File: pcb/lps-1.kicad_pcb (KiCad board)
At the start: 4 copper layers, 75.8 x 30 mm, 24 parts, among them J1 Conn_01x12_Pin, J15 PWR, J2 Conn_01x06_Pin, J4 A_INA219, J5 XBEE, J6 DEV, U1 TC1262-33, U2 ATMega1608_32

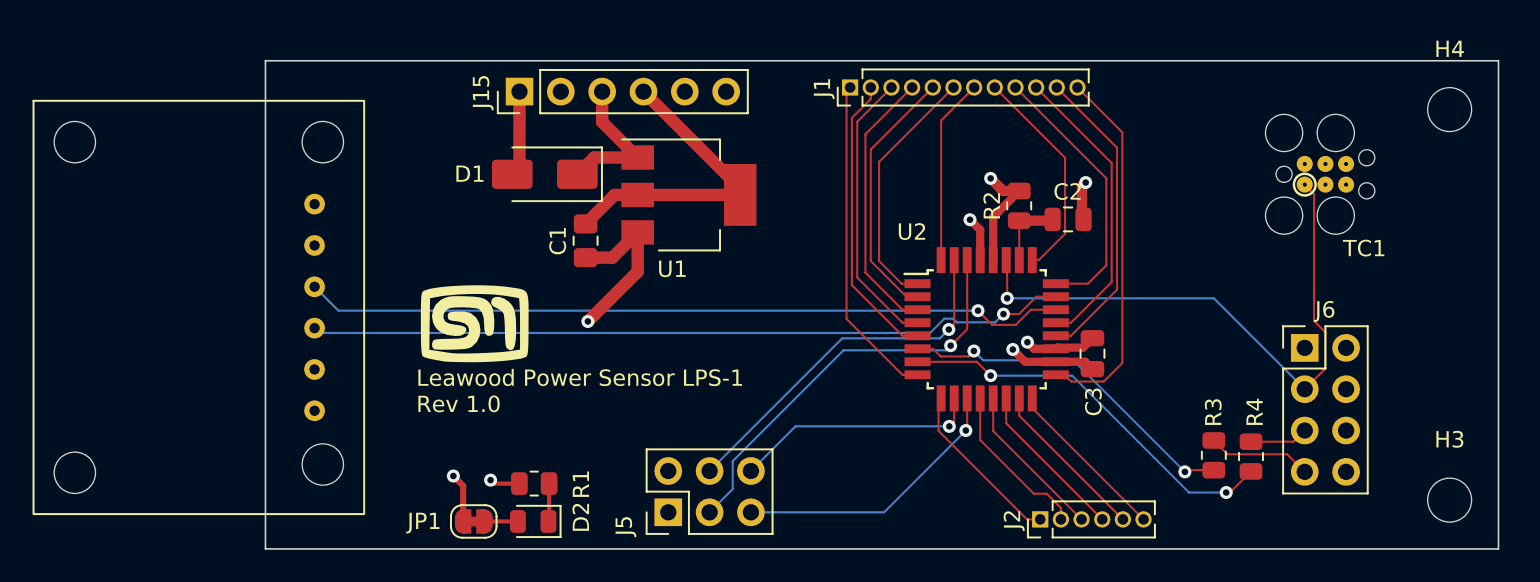
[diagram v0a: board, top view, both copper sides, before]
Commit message: Refactored the connectors for the LPS-X-1
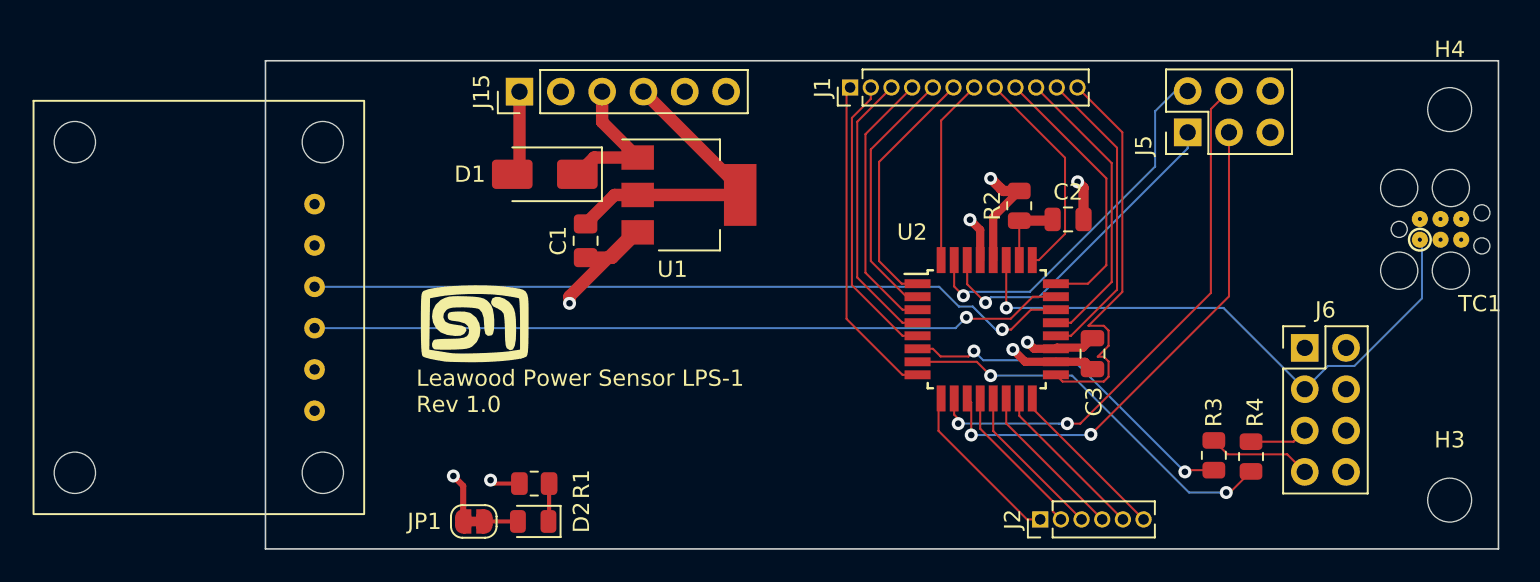
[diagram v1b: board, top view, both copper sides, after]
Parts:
- moved J5 39.5 mm to (125.9, 59.4)
- moved TC1 7.84 mm to (140.2, 66.0)
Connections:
- J5 pad 1: +3.3V -> /TxD0
- J5 pad 2: GND -> /RxD0
- J5 pad 3: /TxD0 -> /MODEM_SLEEP
- J5 pad 4: /RxD0 -> /MODEM_RESET
- J5 pad 5: /MODEM_SLEEP -> +3.3V
- J5 pad 6: /MODEM_RESET -> GND
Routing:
- net /MODEM_RESET: track 15.2 -> 33.4 mm, vias 1 -> 2
- net /MODEM_SLEEP: track 17.3 -> 31.8 mm, vias 1 -> 2
- net /TxD0: track 25.7 -> 20.4 mm
- net /PD7: track 22.8 -> 25.1 mm
- net /RxD0: track 22.7 -> 23.4 mm
- net +3.3V: track 26.0 -> 25.5 mm

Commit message: Reduces the board footprint and introduces copper fills on F and B
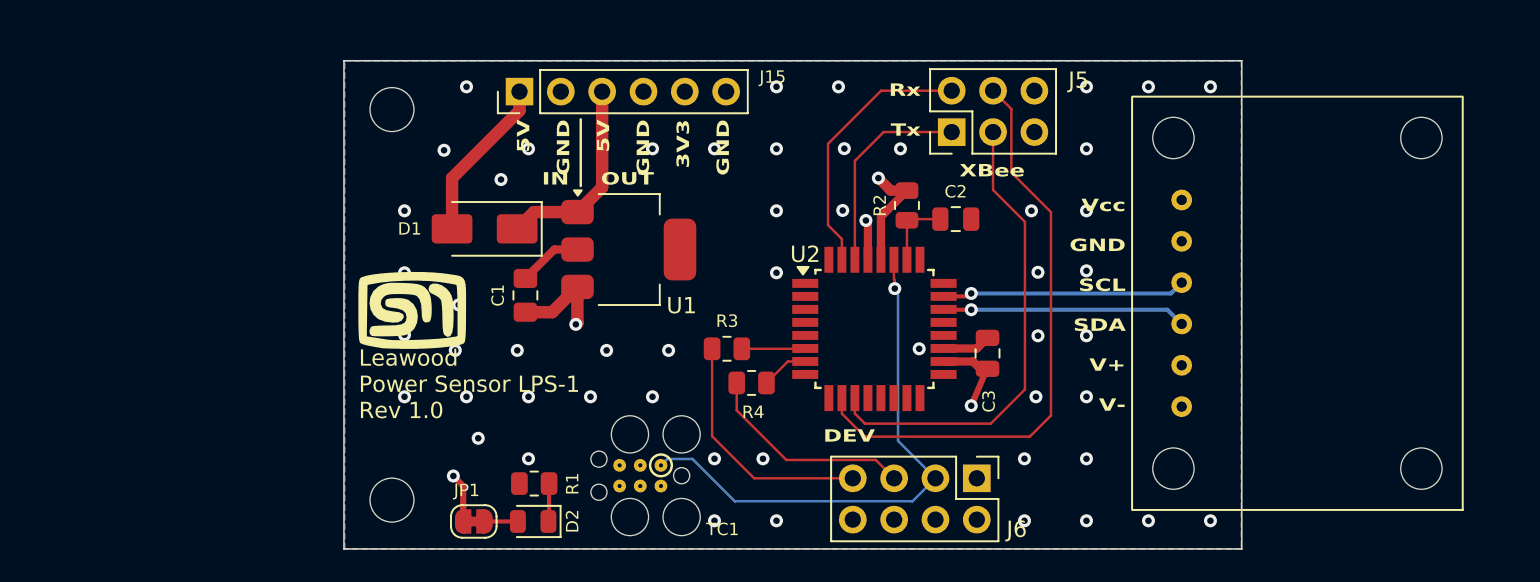
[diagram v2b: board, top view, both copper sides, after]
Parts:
- removed J1: Conn_01x12_Pin, Connector_PinHeader_1.27mm:PinHeader_1x12_P1.27mm_Vertical
- removed J2: Conn_01x06_Pin, Connector_PinHeader_1.27mm:PinHeader_1x06_P1.27mm_Vertical
- moved J4 91.4 mm to (142.8, 82.6), turned to 180 degrees
- moved H3 65.0 mm to (77.0, 82.0)
- moved H4 65.0 mm to (77.0, 58.0)
- moved TC1 48.7 mm to (93.5, 79.9), turned to 180 degrees
- moved Lg3 34.0 mm to (76.3, 69.7), turned to 90 degrees
- moved R4 31.0 mm to (99.1, 74.8), turned to 180 degrees
- moved R3 30.6 mm to (97.6, 72.7), turned to 180 degrees
- moved J6 21.7 mm to (112.9, 80.7), turned to -90 degrees
- moved Lg1 16.3 mm to (114.3, 71.3)
- moved J5 14.5 mm to (111.4, 59.4)
- moved C2 6.90 mm to (111.7, 64.7)
- moved R2 6.90 mm to (108.7, 63.9)
- moved U2 6.90 mm to (106.7, 71.5)
- moved C3 6.45 mm to (113.6, 73.0)
- moved C1 4.99 mm to (85.2, 69.4)
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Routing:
- net /SDA: track 47.2 -> 15.0 mm
- net /SCL: track 46.4 -> 15.0 mm
- net /PD7: track 25.1 -> 0.00 mm
- net Net-(U2-PC1/RxD1-IN1): track 24.4 -> 2.93 mm, vias 2 -> 0
- net GND: track 30.5 -> 9.37 mm, vias 4 -> 53
- net /PC2: track 20.1 -> 0.00 mm
- net /PF0: track 18.9 -> 0.00 mm
- net /PF1: track 18.3 -> 0.00 mm
- net /SS: track 18.0 -> 0.00 mm
- net Net-(U2-PC0/TxD1/2-WO/1-IN0): track 21.7 -> 3.91 mm, vias 2 -> 0
- net /SCK: track 17.4 -> 0.00 mm
- net /PF4: track 16.8 -> 0.00 mm
- net /MISO: track 16.7 -> 0.00 mm
- net /MOSI: track 16.0 -> 0.00 mm
- net /PA3: track 15.5 -> 0.00 mm
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- added copper zone on B.Cu, net GND
- added copper zone on F.Cu, net GND
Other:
- board size 75.8 x 30 mm -> 55.2 x 30 mm
- board text added: "5V GND 5V GND 3V3 GND"
- board text added: "DEV"
- board text added: "IN OUT"
- board text added: "Rx Tx"
- board text added: "Vcc GND SCL SDA V+ V-"
- board text added: "XBee"

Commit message: Rework to include a 5V LDO
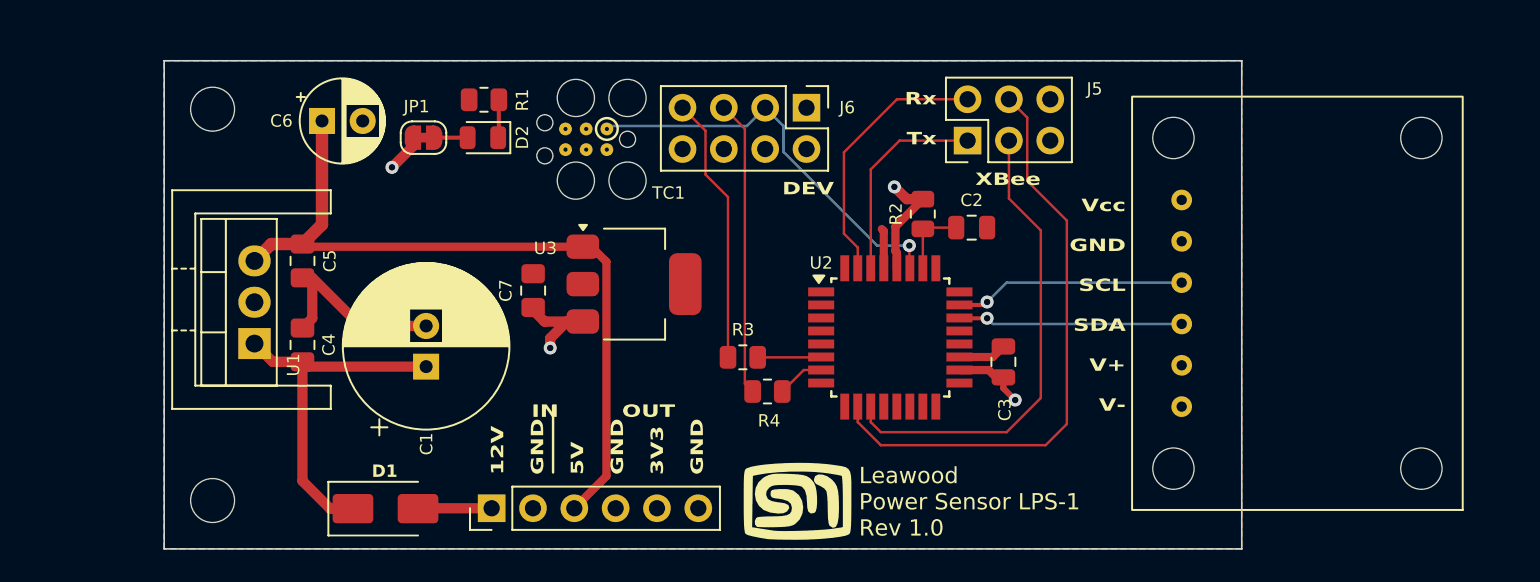
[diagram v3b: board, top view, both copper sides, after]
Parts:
- added C4: 0.1μF, Capacitor_SMD:C_0805_2012Metric_Pad1.18x1.45mm_HandSolder, F.Cu at (71.5, 72.5)
- added C5: 0.1μF, Capacitor_SMD:C_0805_2012Metric_Pad1.18x1.45mm_HandSolder, F.Cu at (71.5, 67.3)
- added C6: 10μF, Capacitor_THT:CP_Radial_D5.0mm_P2.50mm, F.Cu at (72.7, 58.7)
- added C7: 1μF, Capacitor_SMD:C_0805_2012Metric_Pad1.18x1.45mm_HandSolder, F.Cu at (85.7, 69.1)
- added HS1: Heatsink, lps-1-Footprints:Wakefield-E274_13.1x19.3mm, F.Cu at (63.6, 69.7)
- added U3: TC1262-33, Package_TO_SOT_SMD:SOT-223-3_TabPin2, F.Cu at (91.9, 68.7)
- C1: value 1μF -> 220μF; footprint Capacitor_SMD:C_0805_2012Metric_Pad1.18x1.45mm_HandSolder -> Capacitor_THT:CP_Radial_D10.0mm_P2.50mm
- U1: value TC1262-33 -> L7805; footprint Package_TO_SOT_SMD:SOT-223-3_TabPin2 -> Package_TO_SOT_THT:TO-220-3_Vertical
- moved Lg3 41.0 mm to (115.2, 82.4), turned to 180 degrees
- moved Lg2 26.4 mm to (101.9, 82.0)
- moved J15 25.7 mm to (83.1, 82.5)
- moved J6 25.1 mm to (102.5, 57.9)
- moved D2 23.8 mm to (82.6, 59.7)
- moved JP1 23.8 mm to (78.9, 59.7)
- moved R1 23.8 mm to (82.7, 57.4)
- moved U1 23.7 mm to (68.5, 72.4), turned to 90 degrees
- moved TC1 20.9 mm to (90.2, 59.2)
- moved D1 18.2 mm to (76.6, 82.5), turned to 0 degrees
- moved H3 11.0 mm to (66.0, 82.0)
- moved H4 11.0 mm to (66.0, 58.0)
- moved C1 7.51 mm to (79.1, 73.8)
- moved Lg1 1.11 mm to (115.3, 71.8)
- moved R4 1.11 mm to (100.1, 75.3)
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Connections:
- net /5VIN renamed /12VIN
- C1 pad 1: +3.3V -> Net-(D1-K)
- D1 pad 1: +5V -> Net-(D1-K)
- U1 pad 1: +5V -> Net-(D1-K)
- U1 pad 3: +3.3V -> +5V
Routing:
- net +5V: track 12.2 -> 46.5 mm
- net Net-(D1-K): track 0.00 -> 22.3 mm
- net /UPDI: track 33.2 -> 25.0 mm
- net GND: track 9.37 -> 17.0 mm, vias 53 -> 0
- net /12VIN: track 10.2 -> 4.54 mm
- net /DIN: track 13.1 -> 18.2 mm
- net /DOUT: track 15.1 -> 16.5 mm
- net /SDA: track 15.0 -> 13.8 mm
- net +3.3V: track 21.2 -> 20.1 mm
- net /SCL: track 15.0 -> 14.2 mm
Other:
- board size 55.2 x 30 mm -> 66.2 x 30 mm
- board text added: "12V GND 5V GND 3V3 GND"
- board text removed: "5V GND 5V GND 3V3 GND"

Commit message: Reworked the connectors
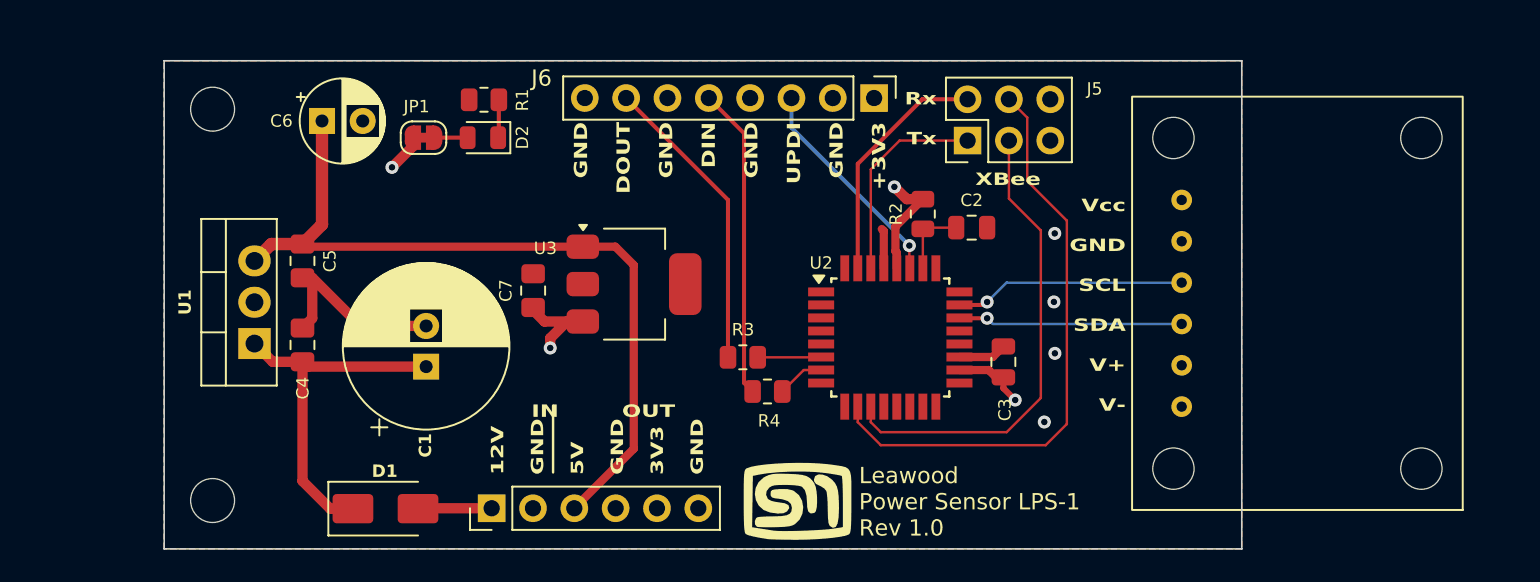
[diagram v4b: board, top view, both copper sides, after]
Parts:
- removed HS1: Heatsink, lps-1-Footprints:Wakefield-E274_13.1x19.3mm
- removed TC1: ISP, TagConnect:PRG_TC2030-IDC-FP_TH
- J6: footprint Connector_PinHeader_2.54mm:PinHeader_2x04_P2.54mm_Vertical -> Connector_PinHeader_2.54mm:PinHeader_1x08_P2.54mm_Vertical
- moved J6 4.20 mm to (106.6, 57.3)
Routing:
- net /UPDI: track 25.0 -> 13.5 mm
- net +5V: track 46.5 -> 48.8 mm
- net /DOUT: track 16.5 -> 18.5 mm
- net /RxD0: track 16.4 -> 14.8 mm
- net /DIN: track 18.2 -> 19.2 mm
- net GND: vias 0 -> 4
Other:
- board text added: "GND DOUT GND DIN GND UPDI GND +3V3"
- board text removed: "DEV"

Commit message: Revision 1.0
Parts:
- J4: footprint lps-1-Footprints:Adafruit-INA219 -> lps-1-Footprints:Adafruit-INA219_2xM2.5
- moved J4 25.7 mm to (125.5, 63.5)
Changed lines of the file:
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@@
 		)
 	)
-	(footprint "lps-1-Footprints:Adafruit-INA219"
+	(footprint "lps-1-Footprints:Adafruit-INA219_2xM2.5"
 		(layer "F.Cu")
-		(at 142.80435 82.605 180)
+		(at 125.524 63.55 180)
 		(property "Reference" "J4"
-			(at 2.54 27.94 180)
+			(at 2.159 7.493 180)
 			(layer "Dwgs.User")
 			(hide yes)
@@
 		)
 		(property "Value" "A_INA219"
-			(at 10.16 12.7 -90)
+			(at 4.064 -6.35 -90)
 			(layer "F.Fab")
 			(effects
@@
 			)
 		)
-		(property "Footprint" "lps-1-Footprints:Adafruit-INA219"
+		(property "Footprint" "lps-1-Footprints:Adafruit-INA219_2xM2.5"
 			(at 0 0 180)
 			(unlocked yes)
@@
 		(attr through_hole)
 		(fp_rect
-			(start 0 0)
-			(end 20.32 25.4)
+			(start -1.794 -19.05)
+			(end 3.032 6.35)
 			(stroke
 				(width 0.12)
@@
 		)
 		(pad "" np_thru_hole circle
-			(at 2.54 2.54 180)
+			(at 0.492 -16.51 180)
 			(size 2.54 2.54)
 			(drill 2.54)
@@
 		)
 		(pad "" np_thru_hole circle
-			(at 2.54 22.86 180)
-			(size 2.54 2.54)
-			(drill 2.54)
-			(layers "F&B.Cu" "*.Mask")
-		)
-		(pad "" np_thru_hole circle
-			(at 17.78 2.54 180)
-			(size 2.54 2.54)
-			(drill 2.54)
-			(layers "F&B.Cu" "*.Mask")
-		)
-		(pad "" np_thru_hole circle
-			(at 17.78 22.86 180)
+			(at 0.492 3.81 180)
 			(size 2.54 2.54)
 			(drill 2.54)
@@
 		)
 		(pad "1" thru_hole circle
-			(at 17.272 19.05 180)
+			(at -0.016 0 180)
 			(size 1.27 1.27)
 			(drill 0.635)
@@
 		)
 		(pad "2" thru_hole circle
-			(at 17.272 16.51 180)
+			(at -0.016 -2.54 180)
 			(size 1.27 1.27)
 			(drill 0.635)
@@
 		)
 		(pad "3" thru_hole circle
-			(at 17.272 13.97 180)
+			(at -0.016 -5.08 180)
 			(size 1.27 1.27)
 			(drill 0.635)
@@
 		)
 		(pad "4" thru_hole circle
-			(at 17.272 11.43 180)
+			(at -0.016 -7.62 180)
 			(size 1.27 1.27)
 			(drill 0.635)
@@
 		)
 		(pad "5" thru_hole circle
-			(at 17.272 8.89 180)
+			(at -0.016 -10.16 180)
 			(size 1.27 1.27)
 			(drill 0.635)
@@
 		)
 		(pad "6" thru_hole circle
-			(at 17.272 6.35 180)
+			(at -0.016 -12.7 180)
 			(size 1.27 1.27)
 			(drill 0.635)
@@
 		(model ":LEAWOOD:Adafruit_INA219/pcb/ina219-dc-current-sensor-1.snapshot.3/CJMCU-219 INA219.step"
 			(offset
-				(xyz 20.32 -25.4 2.54)
+				(xyz 3.032 -6.35 2.54)
 			)
 			(scale
@@
 		(model "${KICAD8_3DMODEL_DIR}/Connector_PinHeader_2.54mm.3dshapes/PinHeader_1x06_P2.54mm_Vertical.step"
 			(offset
-				(xyz 17.145 -19.05 2.54)
+				(xyz -0.143 0 2.54)
 			)
 			(scale
@@
 		)
 		(height -8.36)
-		(gr_text "2606.2992 mils"
+		(gr_text "2.6063 in"
 			(at 96.1 45.49 0)
 			(layer "User.1")
@@
 		)
 		(height -15.96)
-		(gr_text "3454.3307 mils"
+		(gr_text "3.4543 in"
 			(at 98.94 37.87 0)
 			(layer "User.1")
@@
 		)
 		(height -14.58)
-		(gr_text "3937.0079 mils"
+		(gr_text "3.9370 in"
 			(at 100 34.27 0)
 			(layer "User.1")
@@
 		)
 		(height -12.184126)
-		(gr_text "3142.9135 mils"
+		(gr_text "3.1429 in"
 			(at 102.918341 41.675874 359.9856456)
 			(layer "User.1")
@@
 		)
 		(height -16.875)
-		(gr_text "1181.1024 mils"
+		(gr_text "1.1811 in"
 			(at 144.95 70 90)
 			(layer "User.1")
